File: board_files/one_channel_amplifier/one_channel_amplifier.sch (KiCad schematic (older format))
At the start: 27 parts, among them J1 Screw_Terminal_01x02, J2 Screw_Terminal_01x02, J3 Screw_Terminal_01x02, J4 Conn_01x02, J5 Conn_01x02, J6 Screw_Terminal_01x02, U1 LM3886

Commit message: removed silkscreen from U1
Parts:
- U1: footprint Package_TO_SOT_THT:TO-220-11_P3.4x5.08mm_StaggerOdd_Lead4.85mm_Vertical -> one_channel_amplifier:TO-220F-11_P3.4x5.08mm_StaggerOdd_Lead5.08mm_Vertical
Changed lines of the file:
@@
 F 0 "U1" H 5794 3396 50  0000 L CNN
 F 1 "LM3886" H 5794 3305 50  0000 L CNN
-F 2 "Package_TO_SOT_THT:TO-220-11_P3.4x5.08mm_StaggerOdd_Lead4.85mm_Vertical" H 5450 3350 50  0001 C CIN
+F 2 "one_channel_amplifier:TO-220F-11_P3.4x5.08mm_StaggerOdd_Lead5.08mm_Vertical" H 5450 3350 50  0001 C CIN
 F 3 "http://www.ti.com/lit/ds/symlink/lm3886.pdf" H 5450 3350 50  0001 C CNN
 F 4 "LM3886T/NOPB" H 5450 3350 50  0001 C CNN "MPN"

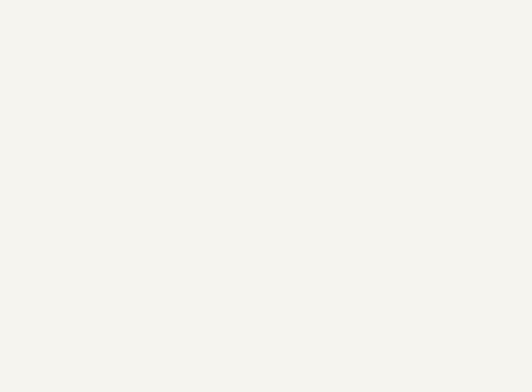
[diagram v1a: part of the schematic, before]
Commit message: Added mounting holes to amplifier PCB
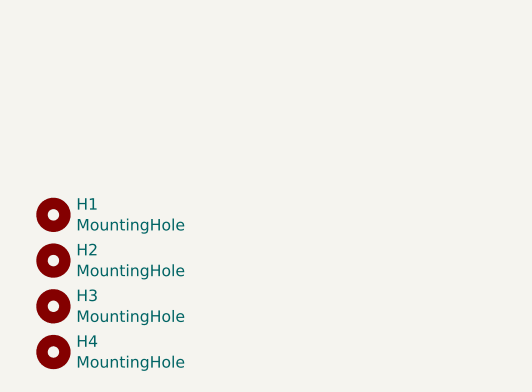
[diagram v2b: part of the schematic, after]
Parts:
- added H1, H2, H3, H4: MountingHole, MountingHole:MountingHole_3.2mm_M3, symbol Mechanical:MountingHole
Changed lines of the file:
@@
 Wire Wire Line
 	1100 1050 1100 1100
+$Comp
+L Mechanical:MountingHole H4
+U 1 1 5EF7D67C
+P 900 6750
+F 0 "H4" H 1000 6796 50  0000 L CNN
+F 1 "MountingHole" H 1000 6705 50  0000 L CNN
+F 2 "MountingHole:MountingHole_3.2mm_M3" H 900 6750 50  0001 C CNN
+F 3 "~" H 900 6750 50  0001 C CNN
+	1    900  6750
+	1    0    0    -1
+$EndComp
+$Comp
+L Mechanical:MountingHole H3
+U 1 1 5EF7F593
+P 900 6550
+F 0 "H3" H 1000 6596 50  0000 L CNN
+F 1 "MountingHole" H 1000 6505 50  0000 L CNN
+F 2 "MountingHole:MountingHole_3.2mm_M3" H 900 6550 50  0001 C CNN
+F 3 "~" H 900 6550 50  0001 C CNN
+	1    900  6550
+	1    0    0    -1
+$EndComp
+$Comp
+L Mechanical:MountingHole H2
+U 1 1 5EF81A4D
+P 900 6350
+F 0 "H2" H 1000 6396 50  0000 L CNN
+F 1 "MountingHole" H 1000 6305 50  0000 L CNN
+F 2 "MountingHole:MountingHole_3.2mm_M3" H 900 6350 50  0001 C CNN
+F 3 "~" H 900 6350 50  0001 C CNN
+	1    900  6350
+	1    0    0    -1
+$EndComp
+$Comp
+L Mechanical:MountingHole H1
+U 1 1 5EF83F07
+P 900 6150
+F 0 "H1" H 1000 6196 50  0000 L CNN
+F 1 "MountingHole" H 1000 6105 50  0000 L CNN
+F 2 "MountingHole:MountingHole_3.2mm_M3" H 900 6150 50  0001 C CNN
+F 3 "~" H 900 6150 50  0001 C CNN
+	1    900  6150
+	1    0    0    -1
+$EndComp
 $EndSCHEMATC
